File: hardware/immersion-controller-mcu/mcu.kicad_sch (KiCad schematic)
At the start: 17 parts, among them J1 COLD, J1 TANK-BOTTOM, J1 TANK-TOP, J4 DISPLAY, J7 RTC, SW1 RotaryEncoder_Switch, U1 ESP32-S3-DevKitC, U2 TOP, U3 BOTTOM, U4 COLD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

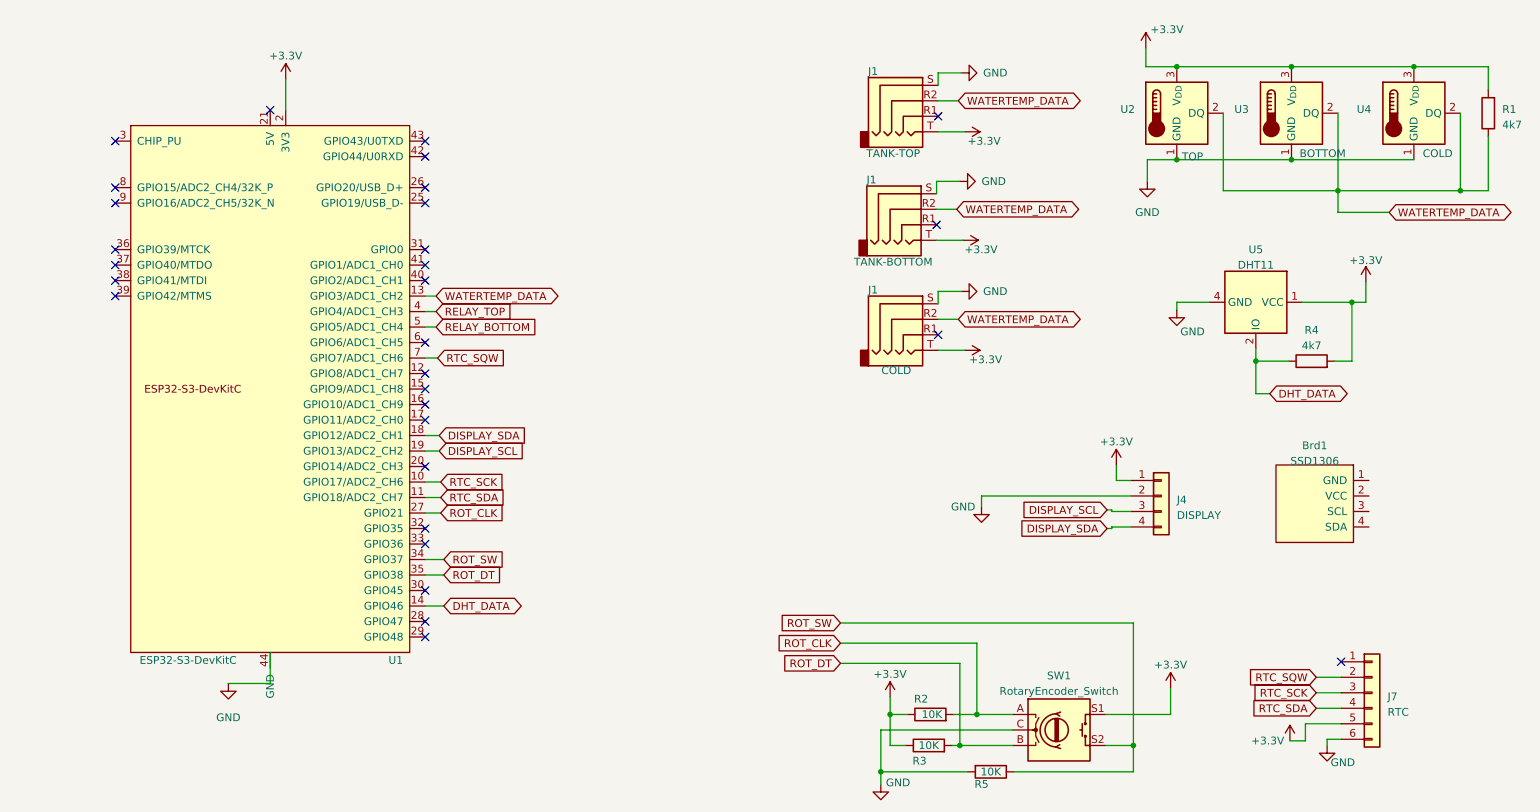
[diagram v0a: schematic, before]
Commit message: Added missing pullup resistor and reset pin
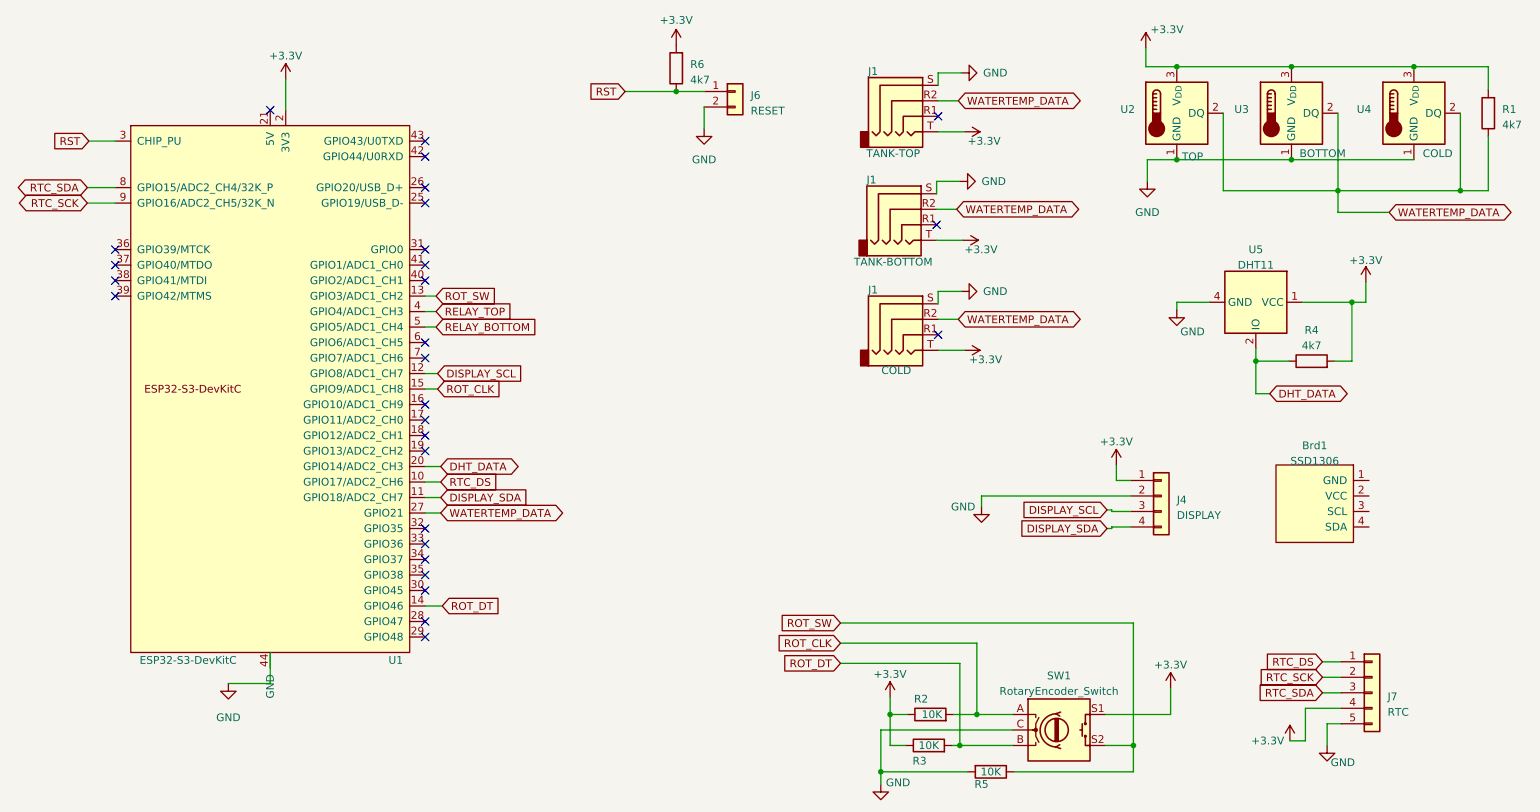
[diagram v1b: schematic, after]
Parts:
- added J6: RESET, Connector_PinHeader_2.54mm:PinHeader_1x02_P2.54mm_Vertical, symbol Connector_Generic:Conn_01x02
- added R6: 4k7, Resistor_SMD:R_0805_2012Metric_Pad1.20x1.40mm_HandSolder, symbol Device:R
- J7: symbol Connector_Generic:Conn_01x06 -> Connector_Generic:Conn_01x05
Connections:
- net +3.3V: now also J7.4 (Pin_4), R6.2; no longer J7.5 (Pin_5)
- net DHT_DATA: now also U1.20 (GPIO14/ADC2_CH3); no longer U1.14 (GPIO46)
- net DISPLAY_SCL: now also U1.12 (GPIO8/ADC1_CH7); no longer U1.19 (GPIO13/ADC2_CH2)
- net DISPLAY_SDA: now also U1.11 (GPIO18/ADC2_CH7); no longer U1.18 (GPIO12/ADC2_CH1)
- net GND: now also J7.5 (Pin_5), J6.2 (Pin_2); no longer J7.6 (Pin_6)
- net ROT_CLK: now also U1.15 (GPIO9/ADC1_CH8); no longer U1.27 (GPIO21)
- net ROT_DT: now also U1.14 (GPIO46); no longer U1.35 (GPIO38)
- net ROT_SW: now also U1.13 (GPIO3/ADC1_CH2); no longer U1.34 (GPIO37)
- net RTC_SCK: now also J7.2 (Pin_2), U1.9 (GPIO16/ADC2_CH5/32K_N); no longer J7.3 (Pin_3), U1.10 (GPIO17/ADC2_CH6)
- net RTC_SDA: now also J7.3 (Pin_3), U1.8 (GPIO15/ADC2_CH4/32K_P); no longer J7.4 (Pin_4), U1.11 (GPIO18/ADC2_CH7)
- net WATERTEMP_DATA: now also U1.27 (GPIO21); no longer U1.13 (GPIO3/ADC1_CH2)
- net RTC_DS: now reaches J7.1 (Pin_1)
- net RTC_DS: now also U1.10 (GPIO17/ADC2_CH6)
- net RST: now reaches U1.3 (CHIP_PU)
- net RST: now also J6.1 (Pin_1), R6.1
- net RTC_SQW: no longer names the net of U1.7 (GPIO7/ADC1_CH6)
- net RTC_SQW: no longer J7.2 (Pin_2)
- no-connect marks 30 -> 28
